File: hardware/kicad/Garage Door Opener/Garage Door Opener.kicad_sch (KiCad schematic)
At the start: 6 parts, among them J1 Conn_01x11_Socket, J3 Screw_Terminal_01x02, J5 HC-SR04, Q1 IRLZ44N

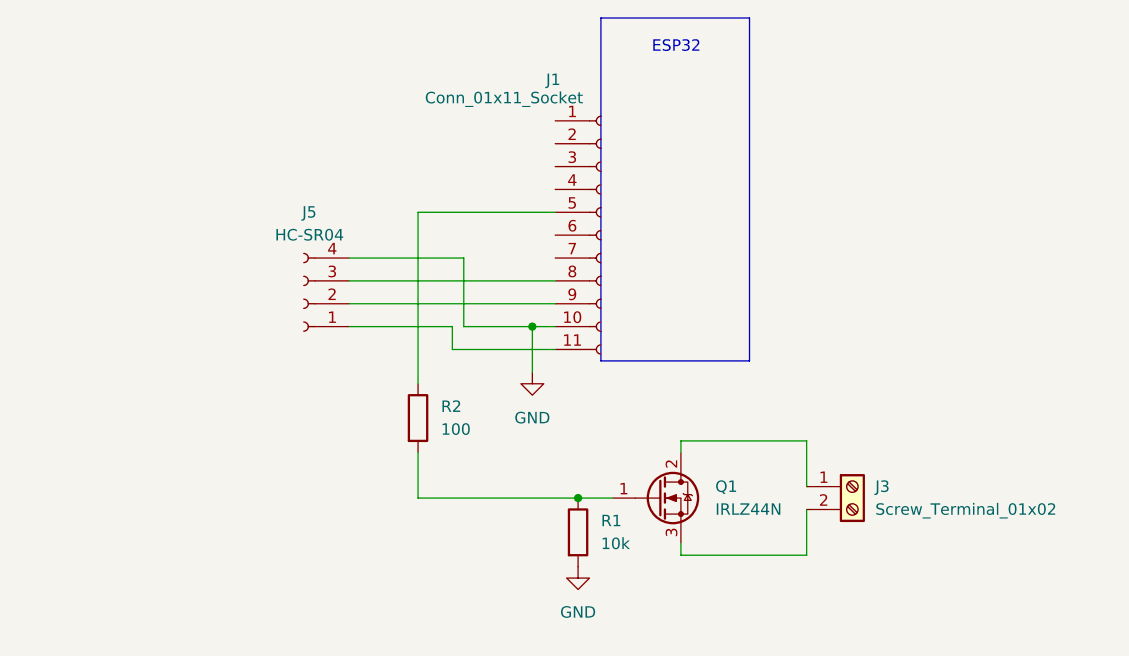
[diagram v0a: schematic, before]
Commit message: Added TVS diode and voltage divider for sonar.
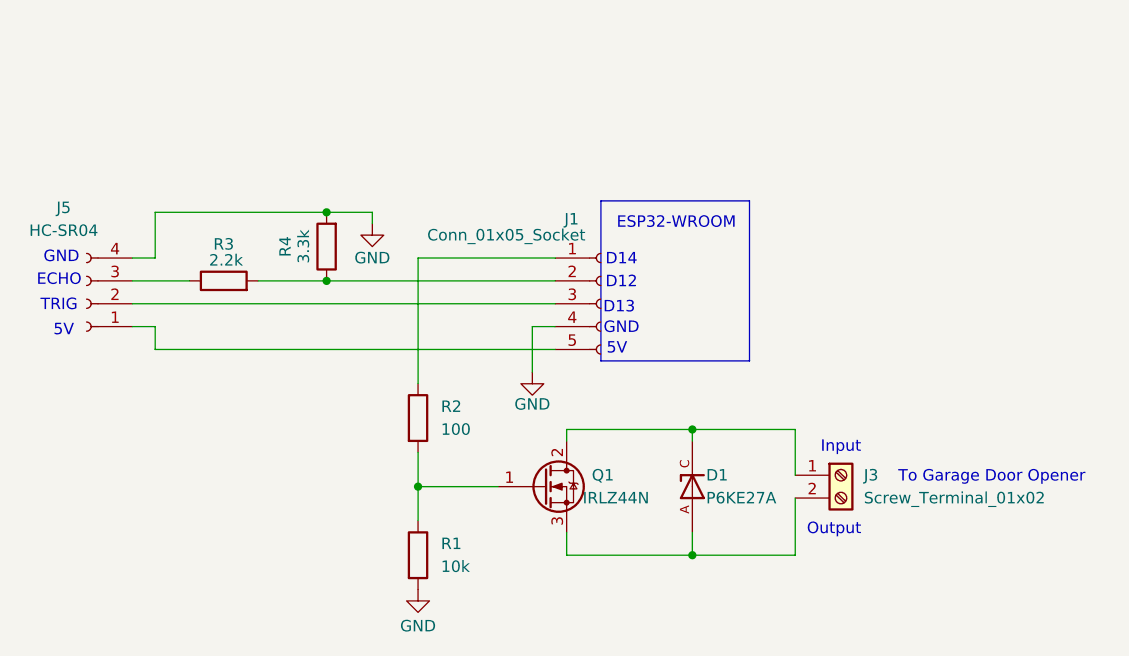
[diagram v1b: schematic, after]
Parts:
- removed J1: Conn_01x11_Socket, Connector_PinSocket_2.54mm:PinSocket_1x11_P2.54mm_Vertical, symbol Connector:Conn_01x11_Socket
- added D1: P6KE27A, P6KE27A:DIOAD1300W80L670D310, symbol P6KE27A:P6KE27A
- added J1: Conn_01x05_Socket, Connector_PinSocket_2.54mm:PinSocket_1x05_P2.54mm_Vertical, symbol Connector:Conn_01x05_Socket
- added R3: 2.2k, Resistor_THT:R_Axial_DIN0309_L9.0mm_D3.2mm_P12.70mm_Horizontal, symbol Device:R
- added R4: 3.3k, Resistor_THT:R_Axial_DIN0309_L9.0mm_D3.2mm_P12.70mm_Horizontal, symbol Device:R
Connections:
- net GND: now also J1.4 (Pin_4), R4.2
- net at J5.1 (Pin_1): now also J1.5 (Pin_5)
- net at J5.2 (Pin_2): now also J1.3 (Pin_3)
- net at J5.3 (Pin_3): now also R3.1
- net at R2.1: now also J1.1 (Pin_1)
- net at J3.1 (Pin_1), Q1.2 (D): now also D1.C
- net at J3.2 (Pin_2), Q1.3 (S): now also D1.A
- new net: J1.2 (Pin_2), R3.2, R4.1
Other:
- note added: "5V"
- note added: "D12"
- note added: "D13"
- note added: "D14"
- note added: "ECHO"
- note added: "ESP32-WROOM"
- note added: "GND"
- note added: "Input"
- note added: "Output"
- note added: "TRIG"
- note added: "To Garage Door Opener"
- note removed: "ESP32"
- moved on the sheet: J3, J5, Q1, R1
